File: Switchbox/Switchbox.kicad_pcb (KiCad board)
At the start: 4 copper layers, 90 x 68 mm, 42 parts, among them J1 USB-C_connector, SW1 SW_SPDT, SW2 SW_SPDT, SW3 SW_SPDT, SW4 SW_SPDT, SW5 SW_SPST_LED, SW6 SW_SPDT_BOX, U2 AP63203WU

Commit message: series of changes
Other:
- copper layers 4 -> 2
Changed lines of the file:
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@@
 	(layers
 		(0 "F.Cu" signal "Front")
-		(4 "In1.Cu" signal)
-		(6 "In2.Cu" signal)
 		(2 "B.Cu" signal "Back")
 		(13 "F.Paste" user)
@@
 			(layer "dielectric 1"
 				(type "core")
-				(thickness 0.480066)
-				(material "FR4")
-				(epsilon_r 4.5)
-				(loss_tangent 0.02)
-			)
-			(layer "In1.Cu"
-				(type "copper")
-				(thickness 0.035)
-			)
-			(layer "dielectric 2"
-				(type "prepreg")
-				(thickness 0.480066)
-				(material "FR4")
-				(epsilon_r 4.5)
-				(loss_tangent 0.02)
-			)
-			(layer "In2.Cu"
-				(type "copper")
-				(thickness 0.035)
-			)
-			(layer "dielectric 3"
-				(type "core")
-				(thickness 0.480066)
+				(thickness 1.510198)
 				(material "FR4")
 				(epsilon_r 4.5)
@@
 		(sheetname "/")
 		(sheetfile "Switchbox.kicad_sch")
-		(attr smd)
+		(attr smd exclude_from_pos_files exclude_from_bom)
 		(fp_line
 			(start 4.15 2.5)
@@
 		(sheetname "/")
 		(sheetfile "Switchbox.kicad_sch")
-		(attr smd)
+		(attr smd exclude_from_pos_files exclude_from_bom)
 		(fp_line
 			(start 4.15 2.5)
@@
 		(sheetname "/")
 		(sheetfile "Switchbox.kicad_sch")
-		(attr smd)
+		(attr smd exclude_from_pos_files exclude_from_bom)
 		(fp_line
 			(start -4.75 -3.275)
@@
 		(sheetname "/")
 		(sheetfile "Switchbox.kicad_sch")
-		(attr smd)
+		(attr smd exclude_from_pos_files exclude_from_bom)
 		(fp_line
 			(start 4.15 2.5)
@@
 		(sheetname "/")
 		(sheetfile "Switchbox.kicad_sch")
-		(attr smd)
+		(attr smd exclude_from_pos_files exclude_from_bom)
 		(fp_line
 			(start -4.75 -3.275)
@@
 		(sheetname "/")
 		(sheetfile "Switchbox.kicad_sch")
-		(attr smd)
+		(attr smd exclude_from_pos_files exclude_from_bom)
 		(fp_line
 			(start 4.15 2.5)
@@
 		(sheetname "/")
 		(sheetfile "Switchbox.kicad_sch")
-		(attr smd)
+		(attr smd exclude_from_pos_files exclude_from_bom)
 		(fp_line
 			(start -4.75 -3.275)
@@
 		(sheetname "/")
 		(sheetfile "Switchbox.kicad_sch")
-		(attr smd)
+		(attr smd exclude_from_pos_files exclude_from_bom)
 		(fp_line
 			(start 4.15 2.5)
@@
 		(sheetname "/")
 		(sheetfile "Switchbox.kicad_sch")
-		(attr smd)
+		(attr smd exclude_from_pos_files exclude_from_bom)
 		(fp_line
 			(start -6.25 -3.25)
@@
 		(sheetname "/")
 		(sheetfile "Switchbox.kicad_sch")
-		(attr smd)
+		(attr smd exclude_from_pos_files exclude_from_bom)
 		(fp_line
 			(start -4.75 -3.275)
@@
 		(sheetname "/")
 		(sheetfile "Switchbox.kicad_sch")
-		(attr smd exclude_from_bom)
+		(attr smd exclude_from_pos_files exclude_from_bom)
 		(fp_line
 			(start 12 -17)
@@
 		(sheetname "/")
 		(sheetfile "Switchbox.kicad_sch")
-		(attr through_hole)
+		(attr through_hole exclude_from_pos_files exclude_from_bom)
 		(fp_line
 			(start 16.64 -3.94)
@@
 		(sheetname "/")
 		(sheetfile "Switchbox.kicad_sch")
-		(attr smd)
+		(attr smd exclude_from_pos_files exclude_from_bom)
 		(fp_line
 			(start -4.75 -3.275)
@@
 		(sheetname "/")
 		(sheetfile "Switchbox.kicad_sch")
-		(attr smd)
+		(attr smd exclude_from_pos_files exclude_from_bom)
 		(fp_line
 			(start 4.15 2.5)

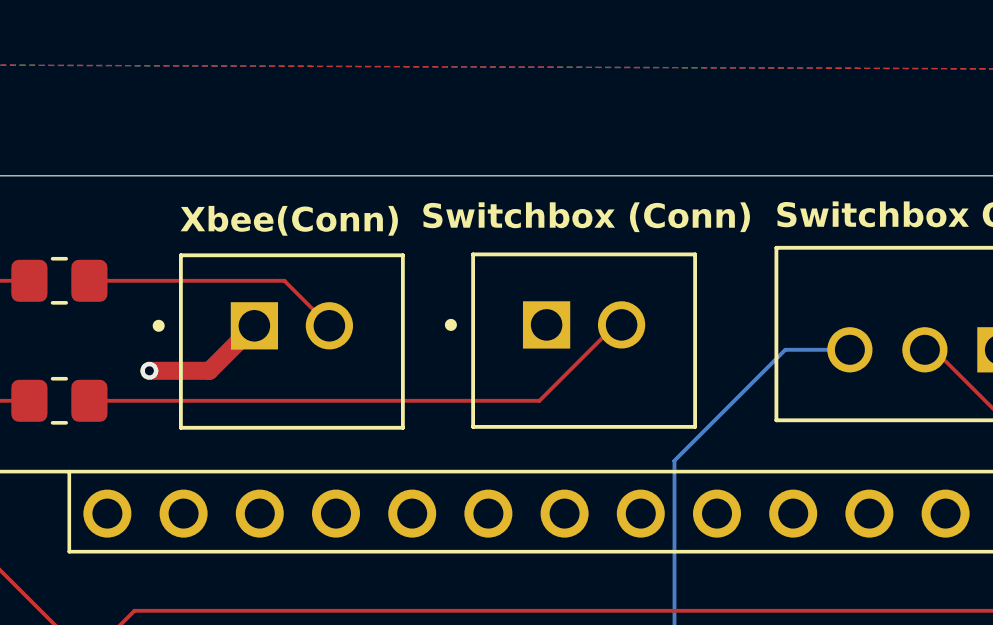
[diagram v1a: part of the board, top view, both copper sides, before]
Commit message: changed usb-c footprint
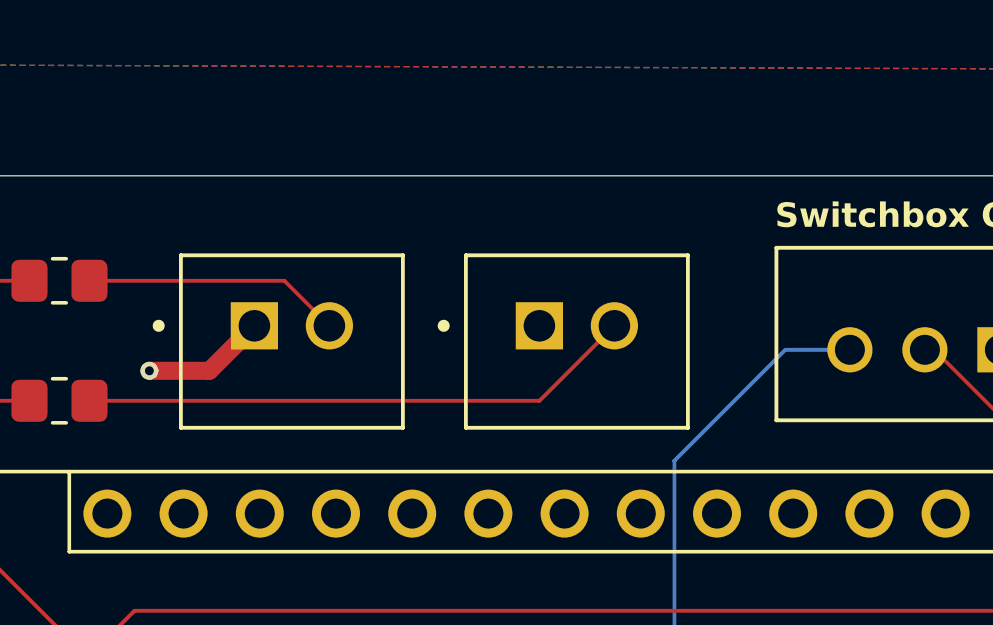
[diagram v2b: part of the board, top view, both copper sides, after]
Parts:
- moved D6 0.24 mm to (165.7, 90.2)
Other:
- copper layers 2 -> 4
- board text removed: "Switchbox (Conn)"
- board text removed: "Xbee(Conn)"
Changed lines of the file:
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@@
 	(layers
 		(0 "F.Cu" signal "Front")
+		(4 "In1.Cu" signal)
+		(6 "In2.Cu" signal)
 		(2 "B.Cu" signal "Back")
 		(13 "F.Paste" user)
@@
 			(layer "dielectric 1"
 				(type "core")
-				(thickness 1.510198)
+				(thickness 0.480066)
+				(material "FR4")
+				(epsilon_r 4.5)
+				(loss_tangent 0.02)
+			)
+			(layer "In1.Cu"
+				(type "copper")
+				(thickness 0.035)
+			)
+			(layer "dielectric 2"
+				(type "prepreg")
+				(thickness 0.480066)
+				(material "FR4")
+				(epsilon_r 4.5)
+				(loss_tangent 0.02)
+			)
+			(layer "In2.Cu"
+				(type "copper")
+				(thickness 0.035)
+			)
+			(layer "dielectric 3"
+				(type "core")
+				(thickness 0.480066)
 				(material "FR4")
 				(epsilon_r 4.5)
@@
 		)
 		(pad_to_mask_clearance 0)
+		(solder_mask_min_width 0.12)
 		(allow_soldermask_bridges_in_footprints no)
 		(tenting front back)
 		(pcbplotparams
-			(layerselection 0x00000000_00000000_55555555_5755f5af)
+			(layerselection 0x00000000_00000000_55555555_5755f5ff)
 			(plot_on_all_layers_selection 0x00000000_00000000_00000000_00000000)
 			(disableapertmacros no)
@@
 			(outputformat 1)
 			(mirror no)
-			(drillshape 0)
+			(drillshape 1)
 			(scaleselection 1)
 			(outputdirectory "")
@@
 	(footprint "switchbox_footprints:2_pin_header"
 		(layer "F.Cu")
-		(at 165.94 90.12 180)
+		(at 165.7 90.15 180)
 		(property "Reference" "D6"
 			(at 0 -0.5 180)
@@
 		(sheetname "/")
 		(sheetfile "Switchbox.kicad_sch")
-		(attr smd exclude_from_pos_files exclude_from_bom)
+		(attr smd)
 		(fp_line
 			(start 4.15 2.5)
@@
 		(sheetname "/")
 		(sheetfile "Switchbox.kicad_sch")
-		(attr smd exclude_from_pos_files exclude_from_bom)
+		(attr smd)
 		(fp_line
 			(start 4.15 2.5)
@@
 		(sheetname "/")
 		(sheetfile "Switchbox.kicad_sch")
-		(attr smd exclude_from_pos_files exclude_from_bom)
+		(attr smd)
 		(fp_line
 			(start -4.75 -3.275)
@@
 		(sheetname "/")
 		(sheetfile "Switchbox.kicad_sch")
-		(attr smd exclude_from_pos_files exclude_from_bom)
+		(attr smd)
 		(fp_line
 			(start 4.15 2.5)
@@
 		(sheetname "/")
 		(sheetfile "Switchbox.kicad_sch")
-		(attr smd exclude_from_pos_files exclude_from_bom)
+		(attr smd)
 		(fp_line
 			(start -4.75 -3.275)
@@
 		(sheetname "/")
 		(sheetfile "Switchbox.kicad_sch")
-		(attr smd exclude_from_pos_files exclude_from_bom)
+		(attr smd)
 		(fp_line
 			(start 4.15 2.5)
@@
 		(sheetname "/")
 		(sheetfile "Switchbox.kicad_sch")
-		(attr smd exclude_from_pos_files exclude_from_bom)
+		(attr smd)
 		(fp_line
 			(start -4.75 -3.275)
@@
 		(sheetname "/")
 		(sheetfile "Switchbox.kicad_sch")
-		(attr smd exclude_from_pos_files exclude_from_bom)
+		(attr smd)
 		(fp_line
 			(start 4.15 2.5)
@@
 		(sheetname "/")
 		(sheetfile "Switchbox.kicad_sch")
-		(attr smd exclude_from_pos_files exclude_from_bom)
+		(attr smd)
 		(fp_line
 			(start -6.25 -3.25)
@@
 		(sheetname "/")
 		(sheetfile "Switchbox.kicad_sch")
-		(attr smd exclude_from_pos_files exclude_from_bom)
+		(attr smd)
 		(fp_line
 			(start -4.75 -3.275)
@@
 		(sheetname "/")
 		(sheetfile "Switchbox.kicad_sch")
-		(attr smd exclude_from_pos_files exclude_from_bom)
+		(attr smd exclude_from_bom)
 		(fp_line
 			(start 12 -17)
@@
 		(sheetname "/")
 		(sheetfile "Switchbox.kicad_sch")
-		(attr through_hole exclude_from_pos_files exclude_from_bom)
+		(attr through_hole)
 		(fp_line
 			(start 16.64 -3.94)
@@
 		(sheetname "/")
 		(sheetfile "Switchbox.kicad_sch")
-		(attr smd exclude_from_pos_files exclude_from_bom)
+		(attr smd)
 		(fp_line
 			(start -4.75 -3.275)
@@
 		(sheetname "/")
 		(sheetfile "Switchbox.kicad_sch")
-		(attr smd exclude_from_pos_files exclude_from_bom)
+		(attr smd)
 		(fp_line
 			(start 4.15 2.5)
@@
 		)
 	)
-	(gr_text "Switchbox (Conn)\n"
-		(at 160.05 86.83 0)
-		(layer "F.SilkS")
-		(effects
-			(font
-				(size 0.8128 0.8128)
-				(thickness 0.1524)
-				(bold yes)
-			)
-			(justify left bottom)
-		)
-	)
 	(gr_text "SW4"
 		(at 176.5 129 0)
@@
 		)
 	)
-	(gr_text "Xbee(Conn)"
-		(at 152.02 86.95 0)
-		(layer "F.SilkS")
-		(effects
-			(font
-				(size 0.8128 0.8128)
-				(thickness 0.1524)
-				(bold yes)
-			)
-			(justify left bottom)
-		)
-	)
 	(gr_text "Arduino Nano\n"
 		(at 163.9 104.05 0)
@@
 		(min_thickness 0.25)
 		(filled_areas_thickness no)
-		(fill yes
+		(fill
 			(thermal_gap 0.5)
 			(thermal_bridge_width 0.5)
